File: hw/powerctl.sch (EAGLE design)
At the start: 15 parts, among them J1 MA02-1, J2 MA03-2, J3 JST-XH-3P, J4 MA02-1, J5 MA02-1

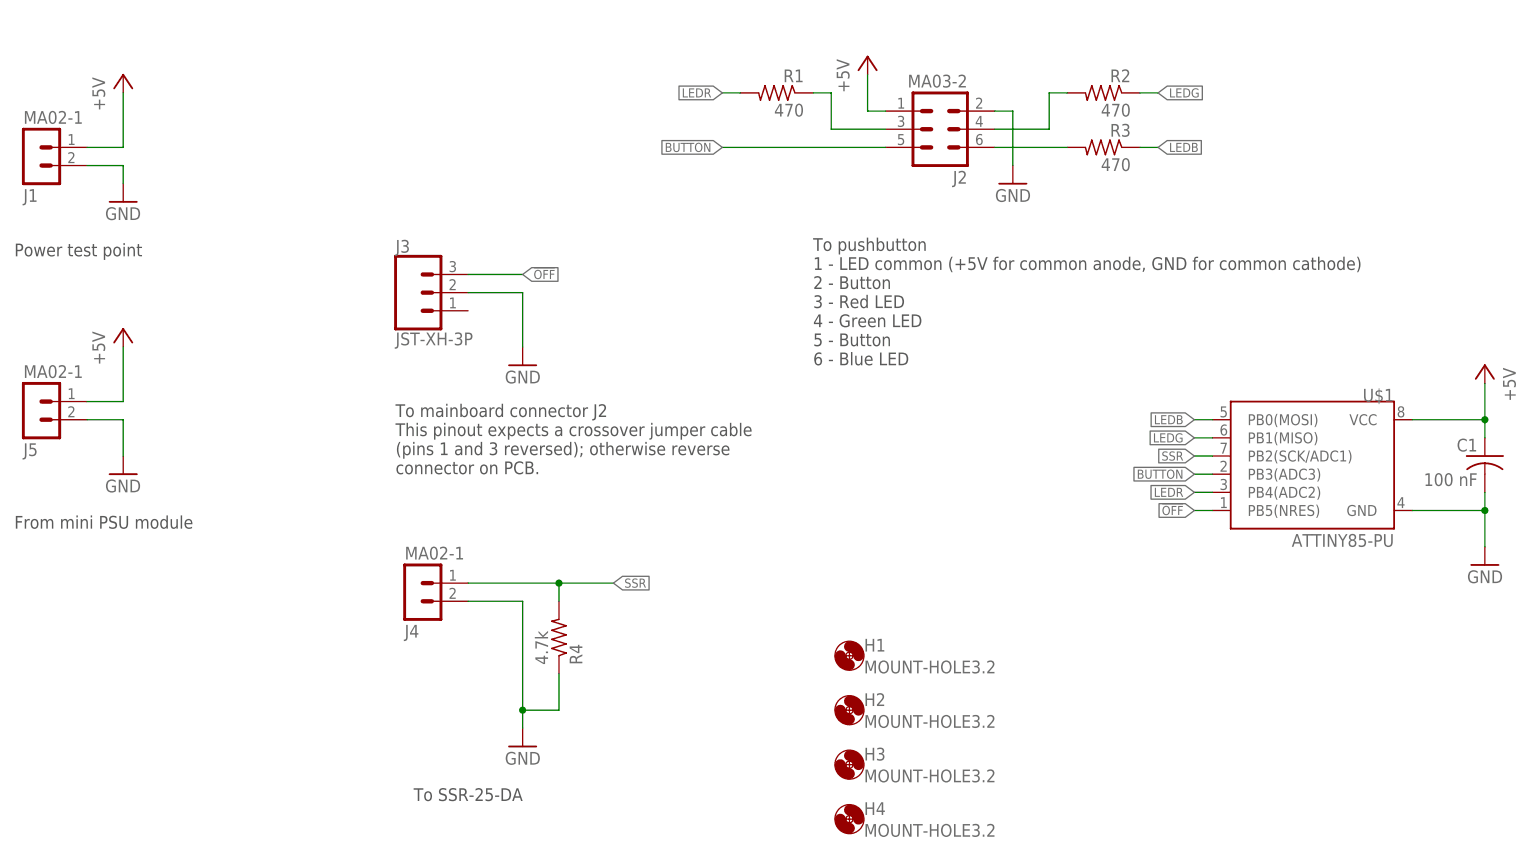
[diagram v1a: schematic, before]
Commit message: Update schematic and add stripboard layout
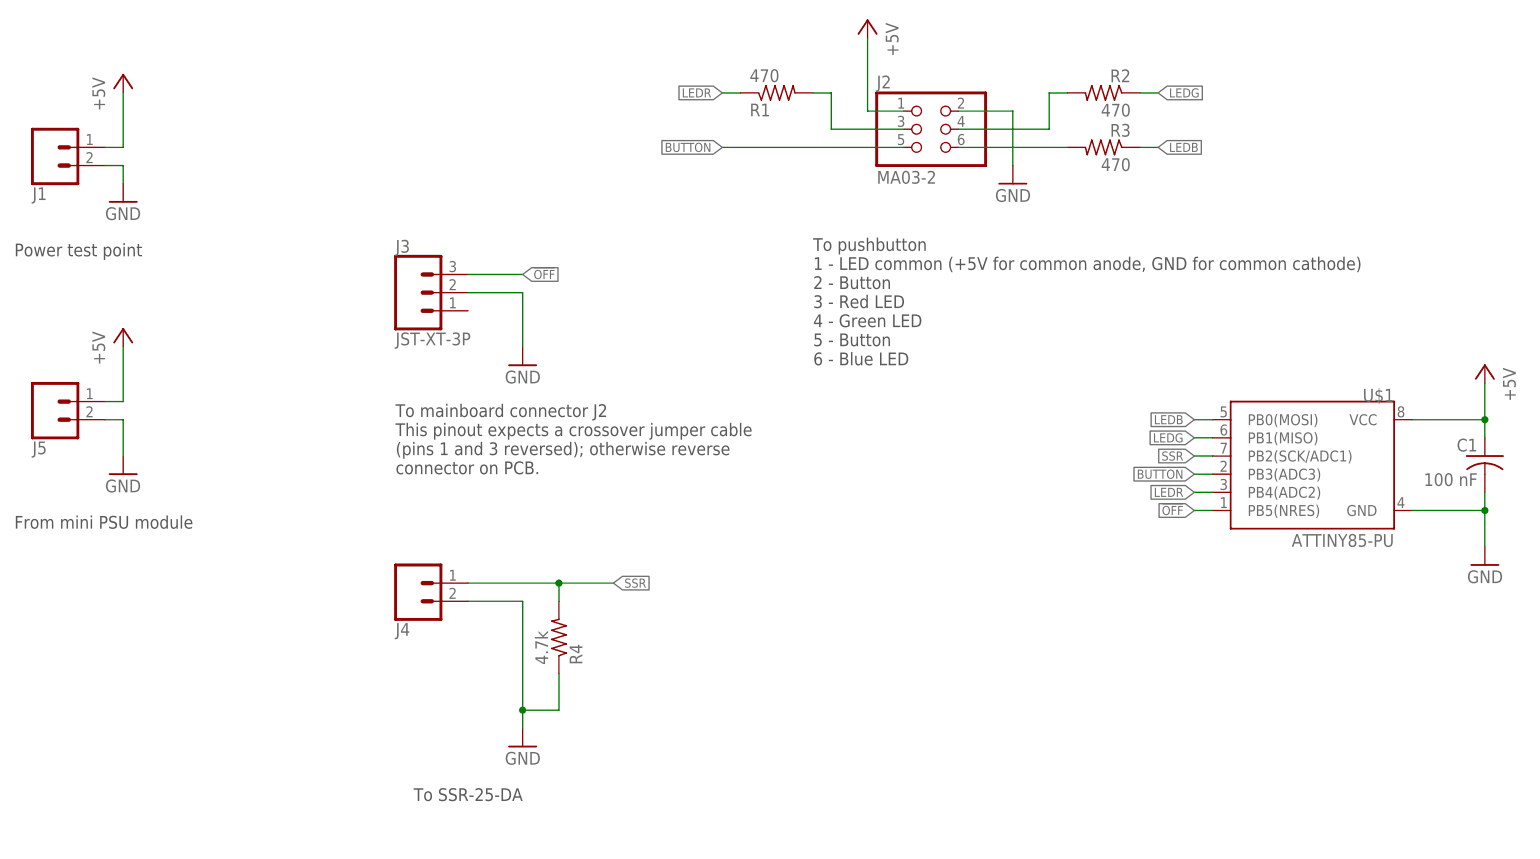
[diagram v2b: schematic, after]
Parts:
- removed H1, H2, H3, H4: MOUNT-HOLE3.2, holes:MOUNT-HOLE3.2
- J1, J4, J5: value MA02-1 -> (none); device con-lstb:MA02-1 -> SparkFun-Connectors:CONN_02
- J2: device con-lstb:MA03-2 -> pinhead:PINHD-2X3
- J3: value JST-XH-3P -> JST-XT-3P; device SparkFun-Connectors:CONN_03JST-PTH-VERT -> SparkFun-Connectors:CONN_03
- R1, R2, R3, R4: device rcl:R-US_0204/7 -> rcl:R-US_0207/15
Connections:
- net LEDR: now also R1.1; no longer R1.2
- net N$2: now also R1.2; no longer R1.1
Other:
- moved on the sheet: J1, J4, J5, R1
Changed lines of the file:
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@@
 <part name="C1" library="rcl" deviceset="C-US" device="025-025X050" value="100 nF"/>
 <part name="GND4" library="supply1" deviceset="GND" device=""/>
-<part name="R1" library="rcl" deviceset="R-US_" device="0204/7" value="470"/>
-<part name="R2" library="rcl" deviceset="R-US_" device="0204/7" value="470"/>
-<part name="R3" library="rcl" deviceset="R-US_" device="0204/7" value="470"/>
+<part name="R1" library="rcl" deviceset="R-US_" device="0207/15" value="470"/>
+<part name="R2" library="rcl" deviceset="R-US_" device="0207/15" value="470"/>
+<part name="R3" library="rcl" deviceset="R-US_" device="0207/15" value="470"/>
 <part name="GND7" library="supply1" deviceset="GND" device=""/>
-<part name="R4" library="rcl" deviceset="R-US_" device="0204/7" value="4.7k"/>
-<part name="J1" library="con-lstb" deviceset="MA02-1" device=""/>
-<part name="J4" library="con-lstb" deviceset="MA02-1" device=""/>
-<part name="J2" library="con-lstb" deviceset="MA03-2" device="" value="MA03-2"/>
-<part name="P+4" library="supply1" deviceset="+5V" device=""/>
+<part name="R4" library="rcl" deviceset="R-US_" device="0207/15" value="4.7k"/>
+<part name="J1" library="SparkFun-Connectors" deviceset="CONN_02" device=""/>
+<part name="J4" library="SparkFun-Connectors" deviceset="CONN_02" device=""/>
+<part name="J2" library="pinhead" deviceset="PINHD-2X3" device="" value="MA03-2"/>
 <part name="GND6" library="supply1" deviceset="GND" device=""/>
-<part name="J3" library="SparkFun-Connectors" deviceset="CONN_03" device="JST-PTH-VERT" value="JST-XH-3P"/>
+<part name="J3" library="SparkFun-Connectors" deviceset="CONN_03" device="" value="JST-XT-3P"/>
 <part name="P+5" library="supply1" deviceset="+5V" device=""/>
 <part name="GND8" library="supply1" deviceset="GND" device=""/>
-<part name="J5" library="con-lstb" deviceset="MA02-1" device=""/>
-<part name="H1" library="holes" deviceset="MOUNT-HOLE" device="3.2"/>
-<part name="H2" library="holes" deviceset="MOUNT-HOLE" device="3.2"/>
-<part name="H3" library="holes" deviceset="MOUNT-HOLE" device="3.2"/>
-<part name="H4" library="holes" deviceset="MOUNT-HOLE" device="3.2"/>
+<part name="J5" library="SparkFun-Connectors" deviceset="CONN_02" device=""/>
+<part name="P+3" library="supply1" deviceset="+5V" device=""/>
 </parts>
 <sheets>
@@
 <instance part="C1" gate="G$1" x="236.22" y="124.46" rot="MR0"/>
 <instance part="GND4" gate="1" x="101.6" y="83.82" rot="MR0"/>
-<instance part="R1" gate="G$1" x="137.16" y="175.26" rot="MR0"/>
+<instance part="R1" gate="G$1" x="137.16" y="175.26" rot="MR180"/>
 <instance part="R2" gate="G$1" x="182.88" y="175.26" rot="MR0"/>
 <instance part="R3" gate="G$1" x="182.88" y="167.64" rot="MR0"/>
 <instance part="GND7" gate="1" x="101.6" y="137.16" rot="MR0"/>
 <instance part="R4" gate="G$1" x="106.68" y="99.06" rot="MR90"/>
-<instance part="J1" gate="G$1" x="33.02" y="165.1" rot="MR180"/>
-<instance part="J4" gate="G$1" x="86.36" y="104.14" rot="MR180"/>
-<instance part="J2" gate="1" x="160.02" y="170.18" rot="R180"/>
-<instance part="P+4" gate="1" x="149.86" y="180.34"/>
+<instance part="J1" gate="G$1" x="35.56" y="167.64" rot="MR180"/>
+<instance part="J4" gate="G$1" x="86.36" y="106.68" rot="MR180"/>
+<instance part="J2" gate="A" x="157.48" y="170.18"/>
 <instance part="GND6" gate="1" x="170.18" y="162.56" rot="MR0"/>
 <instance part="J3" gate="J$1" x="86.36" y="147.32"/>
 <instance part="P+5" gate="1" x="45.72" y="177.8"/>
 <instance part="GND8" gate="1" x="45.72" y="160.02"/>
-<instance part="J5" gate="G$1" x="33.02" y="129.54" rot="MR180"/>
-<instance part="H1" gate="G$1" x="147.32" y="96.52"/>
-<instance part="H2" gate="G$1" x="147.32" y="88.9"/>
-<instance part="H3" gate="G$1" x="147.32" y="81.28"/>
-<instance part="H4" gate="G$1" x="147.32" y="73.66"/>
+<instance part="J5" gate="G$1" x="35.56" y="132.08" rot="MR180"/>
+<instance part="P+3" gate="1" x="149.86" y="185.42" rot="MR0"/>
 </instances>
 <busses>
@@
 <segment>
 <pinref part="P+1" gate="1" pin="+5V"/>
-<wire x1="40.64" y1="132.08" x2="45.72" y2="132.08" width="0.1524" layer="91"/>
+<wire x1="43.18" y1="132.08" x2="45.72" y2="132.08" width="0.1524" layer="91"/>
 <wire x1="45.72" y1="132.08" x2="45.72" y2="139.7" width="0.1524" layer="91"/>
 <pinref part="J5" gate="G$1" pin="1"/>
@@
 </segment>
 <segment>
-<pinref part="J2" gate="1" pin="1"/>
-<wire x1="152.4" y1="172.72" x2="149.86" y2="172.72" width="0.1524" layer="91"/>
-<wire x1="149.86" y1="172.72" x2="149.86" y2="177.8" width="0.1524" layer="91"/>
-<pinref part="P+4" gate="1" pin="+5V"/>
-</segment>
-<segment>
 <pinref part="J1" gate="G$1" pin="1"/>
 <pinref part="P+5" gate="1" pin="+5V"/>
-<wire x1="40.64" y1="167.64" x2="45.72" y2="167.64" width="0.1524" layer="91"/>
+<wire x1="43.18" y1="167.64" x2="45.72" y2="167.64" width="0.1524" layer="91"/>
 <wire x1="45.72" y1="167.64" x2="45.72" y2="175.26" width="0.1524" layer="91"/>
+</segment>
+<segment>
+<pinref part="J2" gate="A" pin="1"/>
+<wire x1="154.94" y1="172.72" x2="149.86" y2="172.72" width="0.1524" layer="91"/>
+<wire x1="149.86" y1="182.88" x2="149.86" y2="172.72" width="0.1524" layer="91"/>
+<pinref part="P+3" gate="1" pin="+5V"/>
 </segment>
 </net>
@@
 <wire x1="45.72" y1="129.54" x2="45.72" y2="124.46" width="0.1524" layer="91"/>
 <pinref part="J5" gate="G$1" pin="2"/>
-<wire x1="45.72" y1="129.54" x2="40.64" y2="129.54" width="0.1524" layer="91"/>
+<wire x1="45.72" y1="129.54" x2="43.18" y2="129.54" width="0.1524" layer="91"/>
 </segment>
 <segment>
@@
 </segment>
 <segment>
-<pinref part="J2" gate="1" pin="2"/>
-<wire x1="167.64" y1="172.72" x2="170.18" y2="172.72" width="0.1524" layer="91"/>
+<pinref part="J2" gate="A" pin="2"/>
+<wire x1="162.56" y1="172.72" x2="170.18" y2="172.72" width="0.1524" layer="91"/>
 <wire x1="170.18" y1="172.72" x2="170.18" y2="165.1" width="0.1524" layer="91"/>
 <pinref part="GND6" gate="1" pin="GND"/>
@@
 <pinref part="J1" gate="G$1" pin="2"/>
 <pinref part="GND8" gate="1" pin="GND"/>
-<wire x1="40.64" y1="165.1" x2="45.72" y2="165.1" width="0.1524" layer="91"/>
+<wire x1="43.18" y1="165.1" x2="45.72" y2="165.1" width="0.1524" layer="91"/>
 <wire x1="45.72" y1="165.1" x2="45.72" y2="162.56" width="0.1524" layer="91"/>
 </segment>
 </net>
-<net name="SSR" class="0">
+<net name="SSR" class="1">
 <segment>
 <wire x1="93.98" y1="106.68" x2="106.68" y2="106.68" width="0.1524" layer="91"/>
@@
 </segment>
 <segment>
-<pinref part="J2" gate="1" pin="5"/>
-<wire x1="152.4" y1="167.64" x2="129.54" y2="167.64" width="0.1524" layer="91"/>
+<pinref part="J2" gate="A" pin="5"/>
+<wire x1="154.94" y1="167.64" x2="129.54" y2="167.64" width="0.1524" layer="91"/>
 <label x="129.54" y="167.64" size="1.27" layer="95" rot="R180" xref="yes"/>
 </segment>
@@
 </segment>
 <segment>
-<pinref part="R1" gate="G$1" pin="2"/>
+<pinref part="R1" gate="G$1" pin="1"/>
 <wire x1="132.08" y1="175.26" x2="129.54" y2="175.26" width="0.1524" layer="91"/>
 <label x="129.54" y="175.26" size="1.27" layer="95" rot="R180" xref="yes"/>
@@
 <net name="N$1" class="0">
 <segment>
-<pinref part="J2" gate="1" pin="6"/>
-<wire x1="167.64" y1="167.64" x2="177.8" y2="167.64" width="0.1524" layer="91"/>
+<pinref part="J2" gate="A" pin="6"/>
+<wire x1="162.56" y1="167.64" x2="177.8" y2="167.64" width="0.1524" layer="91"/>
 <pinref part="R3" gate="G$1" pin="2"/>
 </segment>
@@
 <net name="N$2" class="0">
 <segment>
-<pinref part="R1" gate="G$1" pin="1"/>
+<pinref part="R1" gate="G$1" pin="2"/>
 <wire x1="142.24" y1="175.26" x2="144.78" y2="175.26" width="0.1524" layer="91"/>
 <wire x1="144.78" y1="175.26" x2="144.78" y2="170.18" width="0.1524" layer="91"/>
-<pinref part="J2" gate="1" pin="3"/>
-<wire x1="144.78" y1="170.18" x2="152.4" y2="170.18" width="0.1524" layer="91"/>
+<pinref part="J2" gate="A" pin="3"/>
+<wire x1="144.78" y1="170.18" x2="154.94" y2="170.18" width="0.1524" layer="91"/>
 </segment>
 </net>
 <net name="N$3" class="0">
 <segment>
-<pinref part="J2" gate="1" pin="4"/>
-<wire x1="167.64" y1="170.18" x2="175.26" y2="170.18" width="0.1524" layer="91"/>
+<pinref part="J2" gate="A" pin="4"/>
+<wire x1="162.56" y1="170.18" x2="175.26" y2="170.18" width="0.1524" layer="91"/>
 <wire x1="175.26" y1="170.18" x2="175.26" y2="175.26" width="0.1524" layer="91"/>
 <pinref part="R2" gate="G$1" pin="2"/>
